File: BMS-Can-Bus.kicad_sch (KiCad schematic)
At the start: 55 parts, among them J1 Conn_01x05, J2 Conn_01x02, Q1 dfsg1, Q2 dsg2, Q3 Q_PMOS_GSD, Q4 Q_PMOS_GSD, Q5 Q_PMOS_GSD, Q6 Q_PMOS_GSD, Q7 chg1, Q8 chg2, U1 BQ76952PFB, U2 STM32F103C8Tx, U4 SN65HVD230

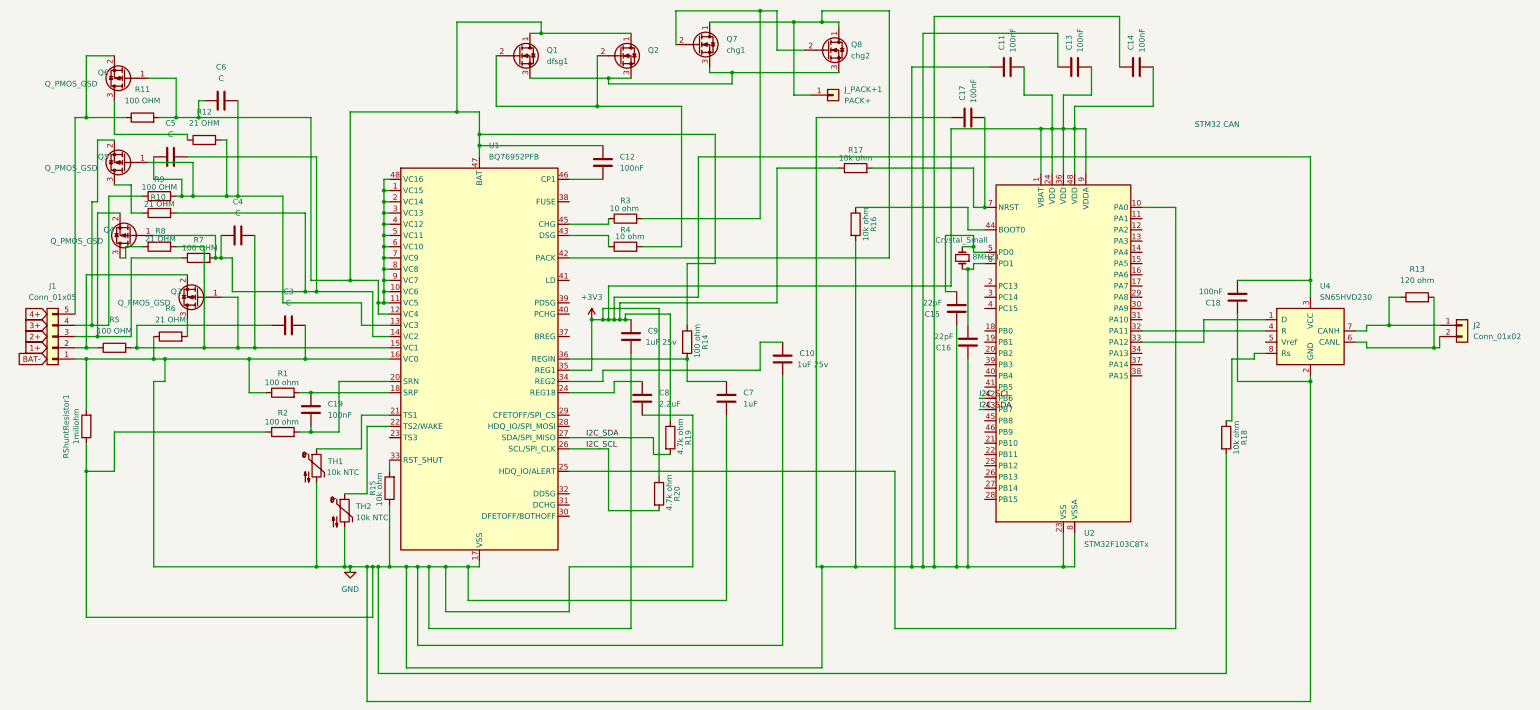
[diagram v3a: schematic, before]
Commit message: shunt resistor bypass add PACK+/- connectors pass DRC
- Fixed shunt resistor bypass issue by isolating BAT- from main GND and properly connecting SRP/SRN Kelvin sense traces.
- Connected PACK+ output terminal to power MOSFETs and routed PACK (Pin 42) & LD (Pin 41) sensing pins with 10k ohm series resistors.
- Added PACK- output connector connected directly to the system GND side of the current shunt.
- Updated PCB netlist from schematic and resolved all DRC short-circuit violations (0 errors, 0 warnings).
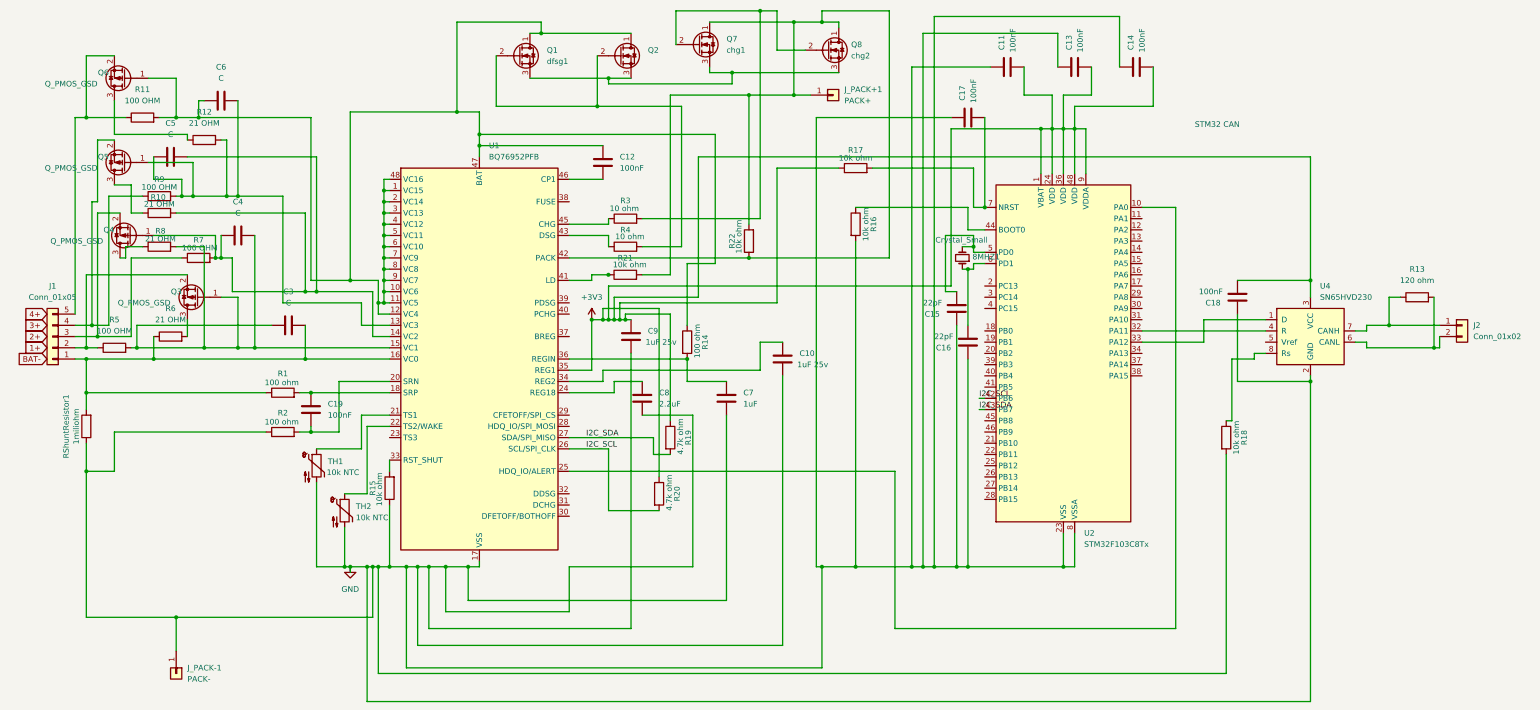
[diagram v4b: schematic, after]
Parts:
- added J_PACK-1: PACK-, MountingHole:MountingHole_5.3mm_M5_Pad, symbol Connector_Generic:Conn_01x01
- added R21, R22: 10k ohm, Resistor_SMD:R_0805_2012Metric, symbol Device:R
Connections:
- net GND: now also J_PACK-1.1 (Pin_1); no longer C3.2, J1.1 (Pin_1), R1.1, R6.1, RShuntResistor1.2, U1.16 (VC0)
- net at J_PACK+1.1 (Pin_1), Q7.1 (D), Q8.1 (D)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: now also R22.1, R22.2
- net at U1.41 (LD): now also R21.1
- new net: C3.2, J1.1 (Pin_1), R1.1, R6.1, RShuntResistor1.2, U1.16 (VC0)
